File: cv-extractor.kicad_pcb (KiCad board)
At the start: 2 copper layers, 40 x 64 mm, 25 parts, among them J1 mono-jack, J2 mono-jack, J3 power_connector_10pos, U1 TL074

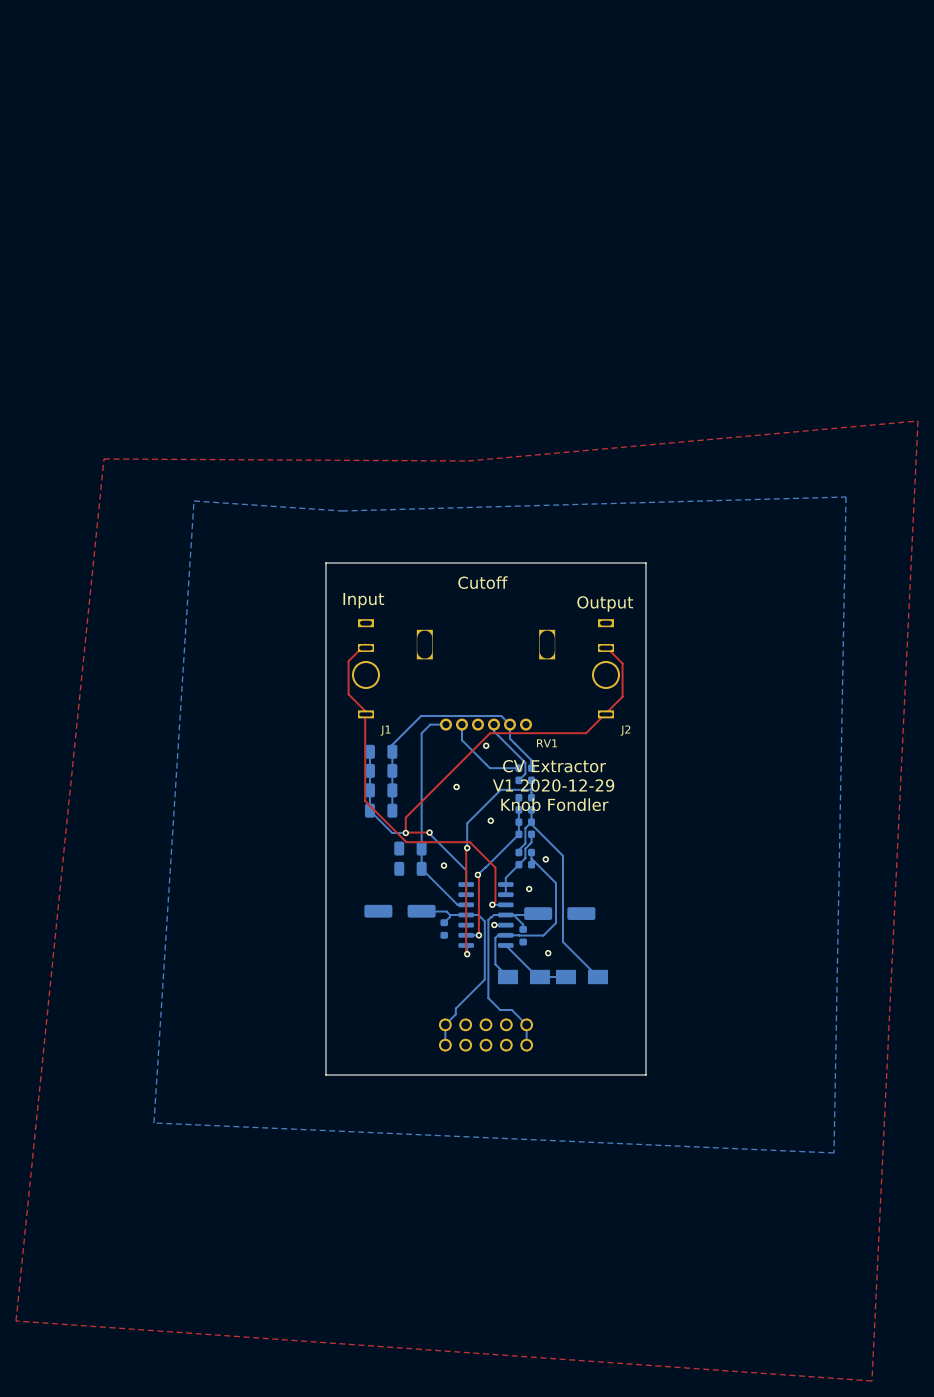
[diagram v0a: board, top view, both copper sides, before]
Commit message: narrower profile, added test points, reduced cutoff range, V2 for fab
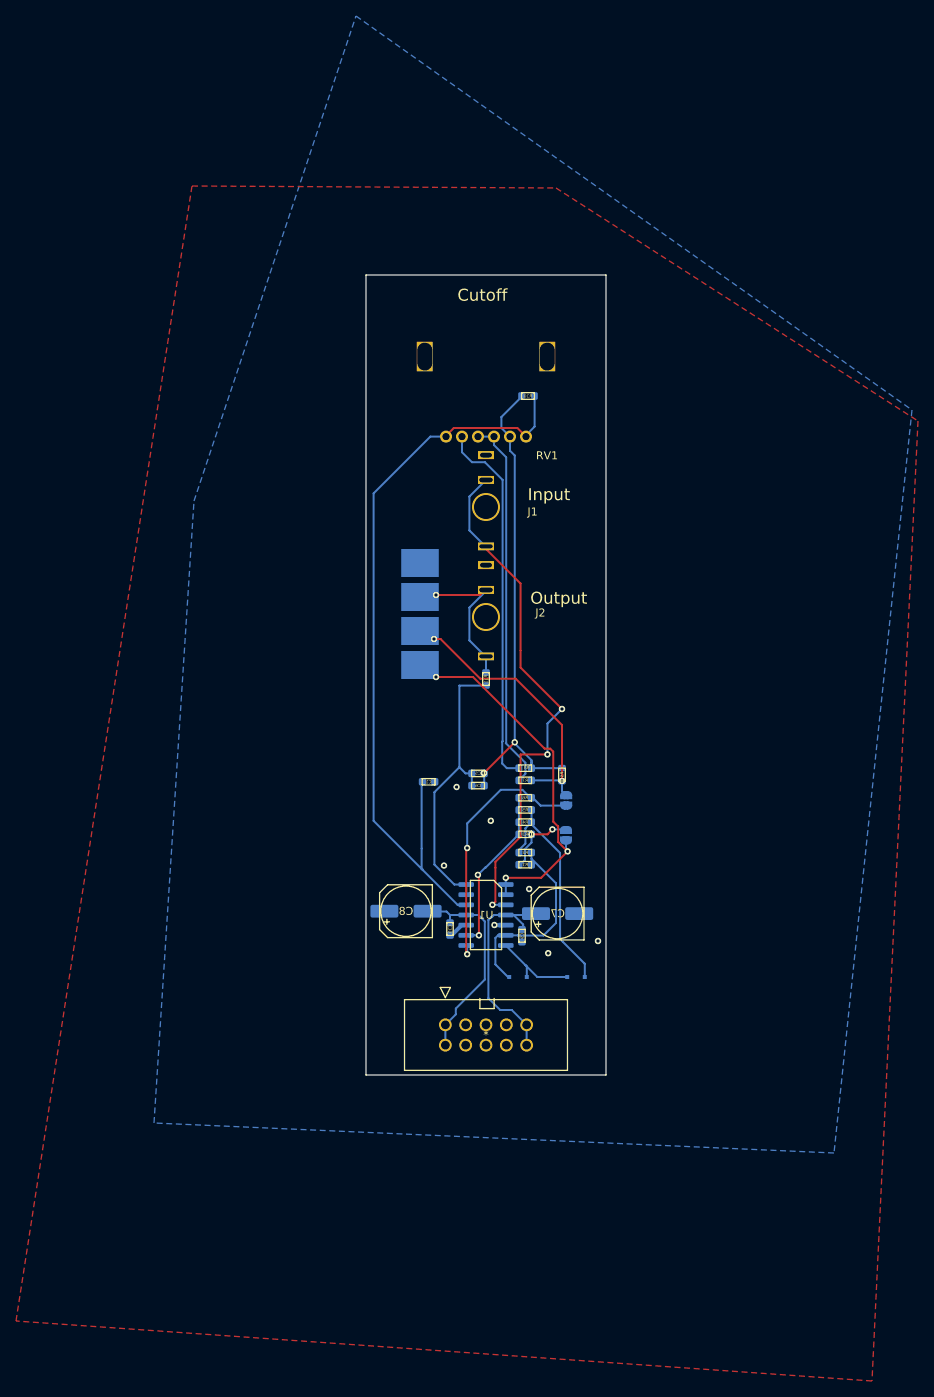
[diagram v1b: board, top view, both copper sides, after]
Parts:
- removed C2, C3, C4: 100uF, Capacitor_SMD:C_1206_3216Metric
- added JP1: SolderJumper_2_Bridged, Jumper:SolderJumper-2_P1.3mm_Open_RoundedPad1.0x1.5mm, B.Cu at (110.0, 90.0)
- added JP2: SolderJumper_2_Bridged, Jumper:SolderJumper-2_P1.3mm_Open_RoundedPad1.0x1.5mm, B.Cu at (110.0, 85.7)
- added R10: 100k, Resistor_SMD:R_0603_1608Metric, B.Cu at (105.2, 35.1)
- added R11: 1k, Resistor_SMD:R_0603_1608Metric, B.Cu at (100.0, 70.5)
- added R9: 100k, Resistor_SMD:R_0603_1608Metric, B.Cu at (109.5, 82.5)
- added TP1: Input, matterwave:TestPoint_TP107, B.Cu at (91.8, 68.8)
- added TP2: Abs, matterwave:TestPoint_TP107, B.Cu at (91.8, 64.5)
- added TP3: Output, matterwave:TestPoint_TP107, B.Cu at (91.8, 60.2)
- added TP4: Abs, matterwave:TestPoint_TP107, B.Cu at (91.8, 56.0)
- C1, C5, C6: value 100uF -> 10uF; footprint Capacitor_SMD:C_1206_3216Metric -> Capacitor_SMD:C_0603_1608Metric
- D1, D2: footprint Diode_SMD:D_SMA -> Diode_SMD:D_SOD-323F
- R7, R8: value 1k -> 2.2k
- moved RV1 36.0 mm to (100.0, 40.2)
- moved J1 25.8 mm to (100.0, 49.0)
- moved J2 16.7 mm to (100.0, 62.8)
- moved C6 12.5 mm to (99.0, 83.8)
- moved C5 12.3 mm to (99.0, 82.3)
- moved C1 8.65 mm to (92.8, 83.3), turned to 180 degrees
- moved C8 0.75 mm to (90.0, 99.5)
- moved D1 0.75 mm to (104.0, 107.8)
- moved D2 0.75 mm to (111.2, 107.8)
- moved C10 0.72 mm to (95.5, 101.8)
- moved C7 0.27 mm to (109.0, 99.8)
- moved C9 0.15 mm to (104.5, 102.6)
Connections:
- C5 pad 2: Net-(C3-Pad2) -> Net-(C5-Pad2)
- C6 pad 2: Net-(C3-Pad2) -> Net-(C5-Pad2)
- J2 pad 2: Net-(C3-Pad2) -> Net-(J2-Pad2)
- J2 pad 3: Net-(C3-Pad2) -> Net-(J2-Pad2)
- R1 pad 2: Net-(R1-Pad2) -> Net-(JP1-Pad2)
- R3 pad 2: Net-(R1-Pad2) -> Net-(JP1-Pad2)
- R6 pad 1: Net-(R6-Pad1) -> Net-(JP2-Pad1)
- R7 pad 2: Net-(R6-Pad1) -> Net-(JP2-Pad2)
- RV1 pad 1: Net-(RV1-Pad1) -> Net-(R7-Pad1)
- RV1 pad 6: Net-(RV1-Pad6) -> Net-(C1-Pad2)
- U1 pad 1: Net-(R1-Pad2) -> Net-(JP1-Pad1)
- U1 pad 13: Net-(C3-Pad2) -> Net-(C5-Pad2)
- U1 pad 14: Net-(C3-Pad2) -> Net-(C5-Pad2)
- U1 pad 2: Net-(R1-Pad2) -> Net-(JP1-Pad1)
- U1 pad 8: Net-(R6-Pad1) -> Net-(JP2-Pad1)
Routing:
- net Net-(C3-Pad2): track 68.8 -> 0.00 mm, vias 2 -> 0
- net Net-(C1-Pad2): track 28.5 -> 96.6 mm
- net Net-(JP1-Pad1): track 0.00 -> 44.4 mm, vias 0 -> 3
- net Net-(R7-Pad1): track 8.96 -> 47.9 mm
- net Net-(C5-Pad2): track 0.00 -> 36.9 mm
- net Net-(R8-Pad1): track 10.5 -> 46.3 mm
- net Net-(JP2-Pad2): track 0.00 -> 33.8 mm, vias 0 -> 2
- net Net-(JP2-Pad1): track 0.00 -> 32.5 mm, vias 0 -> 2
- net Net-(R6-Pad1): track 29.6 -> 0.00 mm, vias 2 -> 0
- net Net-(C5-Pad1): track 31.6 -> 59.9 mm, vias 0 -> 2
- net Net-(J1-Pad2): track 47.5 -> 66.1 mm, vias 1 -> 3
- net Net-(J2-Pad2): track 0.00 -> 18.1 mm, vias 0 -> 1
- net Net-(JP1-Pad2): track 0.00 -> 9.52 mm, vias 0 -> 2
- net Net-(R1-Pad2): track 9.16 -> 0.00 mm
- net GND: track 1.64 -> 5.61 mm, vias 8 -> 7
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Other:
- board size 40 x 64 mm -> 30 x 100 mm
- board text added: "-12V"
- board text added: "CV Extractor V2 2021-10-29 Knob Fondler"
- board text removed: "CV Extractor V1 2020-12-29 Knob Fondler"

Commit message: havent been good about commits, its at V4 now
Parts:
- removed R10: 100k, Resistor_SMD:R_0603_1608Metric
- removed R11: 1k, Resistor_SMD:R_0603_1608Metric
- added H1: Hole, MountingHole:MountingHole_3.2mm_M3, F.Cu at (111.5, 61.0)
- added H2: Hole, MountingHole:MountingHole_3.2mm_M3, F.Cu at (88.5, 61.0)
- added R12: 1k, Resistor_SMD:R_0603_1608Metric, B.Cu at (105.3, 46.7)
- added RD1: 1M, Resistor_SMD:R_0603_1608Metric, B.Cu at (97.3, 24.2)
- added RV2: 10k, matterwave:pot_bourns_PTV09, F.Cu at (100.0, 39.7)
- added RV3: 10k, matterwave:pot_bourns_PTV09, F.Cu at (100.0, 55.0)
- C1, C5, C6: value 10uF -> 470nF
- J1: value mono-jack -> Wave In
- J2: value mono-jack -> CV Out
- R7, R8: value 2.2k -> 1k
- R9: value 100k -> 1k
- TP4: value Abs -> GND
- moved J2 41.0 mm to (100.0, 103.8)
- moved RV1 40.3 mm to (100.0, 80.5)
- moved R9 25.3 mm to (94.8, 61.9), turned to 0 degrees
- moved C7 24.2 mm to (90.7, 83.8), turned to 180 degrees
- moved D2 23.5 mm to (107.5, 84.6)
- moved D1 23.1 mm to (104.2, 84.6)
- moved TP1 22.3 mm to (88.5, 46.7)
- moved J1 21.5 mm to (100.0, 27.5)
- moved C9 18.2 mm to (100.8, 84.8), turned to 180 degrees
- moved TP4 16.6 mm to (88.5, 39.7)
- moved C1 13.9 mm to (105.9, 78.7), turned to 0 degrees
- moved R6 12.5 mm to (112.2, 95.5), turned to 0 degrees
- moved C6 10.8 mm to (100.3, 73.1)
- moved U1 10.6 mm to (99.8, 89.4), turned to 270 degrees
- moved TP2 10.2 mm to (88.5, 54.8)
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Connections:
- J2 pad 2: Net-(J2-Pad2) -> Net-(C5-Pad2)
- J2 pad 3: Net-(J2-Pad2) -> Net-(C5-Pad2)
- R9 pad 1: Net-(C5-Pad1) -> GND
- R9 pad 2: Net-(JP2-Pad2) -> Net-(R9-Pad2)
- TP3 pad 1: Net-(J2-Pad2) -> Net-(C5-Pad2)
- U1 pad 13: Net-(C5-Pad2) -> Net-(RV3-Pad2)
- U1 pad 2: Net-(JP1-Pad1) -> Net-(R12-Pad2)
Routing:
- net Net-(R12-Pad2): track 0.00 -> 65.0 mm, vias 0 -> 2
- net Net-(C1-Pad2): track 96.6 -> 31.8 mm, vias 0 -> 1
- net Net-(C5-Pad2): track 36.9 -> 97.9 mm, vias 0 -> 4
- net Net-(RV3-Pad2): track 0.00 -> 51.8 mm, vias 0 -> 2
- net Net-(C5-Pad1): track 59.9 -> 12.4 mm, vias 2 -> 1
- net Net-(R8-Pad1): track 46.3 -> 3.50 mm
- net Net-(R7-Pad1): track 47.9 -> 6.55 mm
- net Net-(JP1-Pad1): track 44.4 -> 81.2 mm
- net Net-(J1-Pad2): track 66.1 -> 90.3 mm, vias 3 -> 0
- net Net-(J2-Pad2): track 18.1 -> 0.00 mm, vias 1 -> 0
- net +12V: track 29.3 -> 45.6 mm, vias 0 -> 1
- net Net-(D2-Pad2): track 28.1 -> 14.6 mm
- net -12V: track 27.5 -> 40.8 mm
- net Net-(D1-Pad1): track 24.7 -> 14.2 mm
- net Net-(JP2-Pad1): track 32.5 -> 39.7 mm, vias 2 -> 0
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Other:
- outline, holes or cut-outs redrawn
- board text added: "CV Extractor V4 2022-04-20 Knob Fondler"
- board text removed: "-12V"
- board text removed: "CV Extractor V2 2021-10-29 Knob Fondler"
- board text removed: "Cutoff"
- board text removed: "Input"
- board text removed: "Output"
